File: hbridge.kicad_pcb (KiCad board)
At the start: 4 copper layers, 31.8 x 62.7 mm, 29 parts, among them J11 Conn_01x06_Male, J12 Screw_Terminal_01x04, J21 Conn_01x03_Male, J22 Conn_01x06_Female, Q1 2N7000, Q11 2N7000, Q13 2N3904, Q14 2N3906, Q15 2N3904, Q16 2N3906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

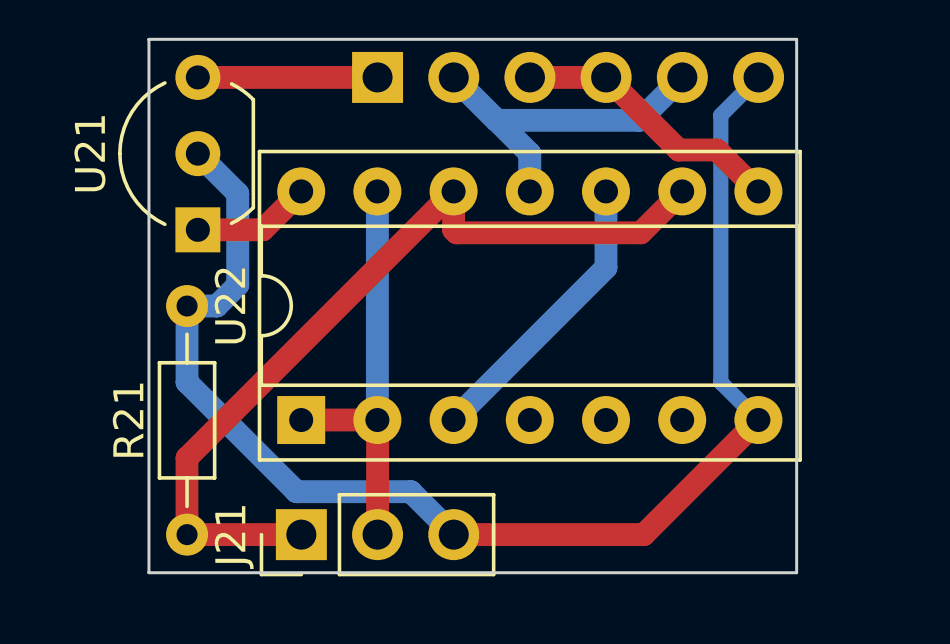
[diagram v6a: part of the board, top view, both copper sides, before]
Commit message: Added bypass cap, tied unused inputs to gnd
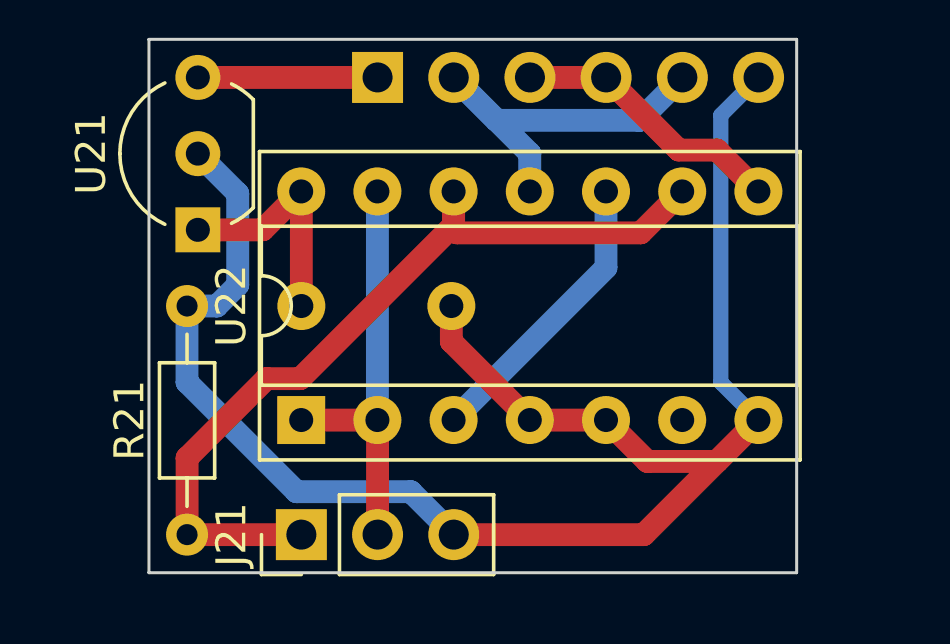
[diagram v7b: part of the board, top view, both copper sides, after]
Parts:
- added C21: 0.1u, Capacitor_THT:C_Disc_D4.3mm_W1.9mm_P5.00mm, B.Cu at (106.7, 109.2)
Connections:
- U22 pad 4: (no net) -> GND
- U22 pad 5: (no net) -> GND
- U22 pad 6: (no net) -> unconnected-(U22-Pad6)
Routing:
- net GND: track 163.0 -> 176.7 mm
- net +5V: track 3.98 -> 7.80 mm
- net /EN: track 28.4 -> 29.1 mm
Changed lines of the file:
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@@
   (net 17 "/DIR")
   (net 18 "Net-(U22-Pad10)")
+  (net 19 "unconnected-(U22-Pad6)")
   (footprint "Package_TO_SOT_THT:TO-220-3_Vertical" (layer "F.Cu")
     (at 115.245 80.01 90)
@@
     (pad "3" thru_hole oval (at 0 5.08 90) (size 1.6 1.6) (drill 0.8) (layers *.Cu *.Mask)
       (net 18 "Net-(U22-Pad10)") (pintype "output"))
-    (pad "4" thru_hole oval (at 0 7.62 90) (size 1.6 1.6) (drill 0.8) (layers *.Cu *.Mask))
-    (pad "5" thru_hole oval (at 0 10.16 90) (size 1.6 1.6) (drill 0.8) (layers *.Cu *.Mask))
-    (pad "6" thru_hole oval (at 0 12.7 90) (size 1.6 1.6) (drill 0.8) (layers *.Cu *.Mask))
+    (pad "4" thru_hole oval (at 0 7.62 90) (size 1.6 1.6) (drill 0.8) (layers *.Cu *.Mask)
+      (net 2 "GND") (pintype "input"))
+    (pad "5" thru_hole oval (at 0 10.16 90) (size 1.6 1.6) (drill 0.8) (layers *.Cu *.Mask)
+      (net 2 "GND") (pintype "input"))
+    (pad "6" thru_hole oval (at 0 12.7 90) (size 1.6 1.6) (drill 0.8) (layers *.Cu *.Mask)
+      (net 19 "unconnected-(U22-Pad6)") (pintype "output+no_connect"))
     (pad "7" thru_hole oval (at 0 15.24 90) (size 1.6 1.6) (drill 0.8) (layers *.Cu *.Mask)
       (net 2 "GND") (pinfunction "GND") (pintype "power_in"))
@@
     )
   )
+  (footprint "Capacitor_THT:C_Disc_D4.3mm_W1.9mm_P5.00mm" (layer "B.Cu")
+    (at 106.68 109.22)
+    (descr "C, Disc series, Radial, pin pitch=5.00mm, , diameter*width=4.3*1.9mm^2, Capacitor, http://www.vishay.com/docs/45233/krseries.pdf")
+    (tags "C Disc series Radial pin pitch 5.00mm  diameter 4.3mm width 1.9mm Capacitor")
+    (property "Sheetfile" "logic.kicad_sch")
+    (property "Sheetname" "control_logic")
+    (attr through_hole)
+    (fp_text reference "C21" (at 2.5 2.2) (layer "B.SilkS")
+      (effects (font (size 1 1) (thickness 0.15)) (justify mirror))
+    )
+    (fp_text value "0.1u" (at 2.5 -2.2) (layer "B.Fab")
+      (effects (font (size 1 1) (thickness 0.15)) (justify mirror))
+    )
+    (fp_text user "${REFERENCE}" (at 2.5 0) (layer "B.Fab")
+      (effects (font (size 0.86 0.86) (thickness 0.129)) (justify mirror))
+    )
+    (fp_line (start 0.23 -1.055) (end 0.23 -1.07) (layer "B.SilkS") (width 0.12))
+    (fp_line (start 0.23 1.07) (end 0.23 1.055) (layer "B.SilkS") (width 0.12))
+    (fp_line (start 4.77 -1.055) (end 4.77 -1.07) (layer "B.SilkS") (width 0.12))
+    (fp_line (start 4.77 1.07) (end 4.77 1.055) (layer "B.SilkS") (width 0.12))
+    (fp_line (start 0.23 -1.07) (end 4.77 -1.07) (layer "B.SilkS") (width 0.12))
+    (fp_line (start 0.23 1.07) (end 4.77 1.07) (layer "B.SilkS") (width 0.12))
+    (fp_line (start -1.05 1.2) (end -1.05 -1.2) (layer "B.CrtYd") (width 0.05))
+    (fp_line (start 6.05 1.2) (end -1.05 1.2) (layer "B.CrtYd") (width 0.05))
+    (fp_line (start 6.05 -1.2) (end 6.05 1.2) (layer "B.CrtYd") (width 0.05))
+    (fp_line (start -1.05 -1.2) (end 6.05 -1.2) (layer "B.CrtYd") (width 0.05))
+    (fp_line (start 4.65 -0.95) (end 4.65 0.95) (layer "B.Fab") (width 0.1))
+    (fp_line (start 0.35 -0.95) (end 4.65 -0.95) (layer "B.Fab") (width 0.1))
+    (fp_line (start 0.35 0.95) (end 0.35 -0.95) (layer "B.Fab") (width 0.1))
+    (fp_line (start 4.65 0.95) (end 0.35 0.95) (layer "B.Fab") (width 0.1))
+    (pad "1" thru_hole circle (at 0 0) (size 1.6 1.6) (drill 0.8) (layers *.Cu *.Mask)
+      (net 4 "+5V") (pintype "passive"))
+    (pad "2" thru_hole circle (at 5 0) (size 1.6 1.6) (drill 0.8) (layers *.Cu *.Mask)
+      (net 2 "GND") (pintype "passive"))
+    (model "${KICAD6_3DMODEL_DIR}/Capacitor_THT.3dshapes/C_Disc_D4.3mm_W1.9mm_P5.00mm.wrl"
+      (offset (xyz 0 0 0))
+      (scale (xyz 1 1 1))
+      (rotate (xyz 0 0 0))
+    )
+  )
   (footprint "Capacitor_SMD:C_0603_1608Metric" (layer "B.Cu")
     (at 114.3 57.263 -90)
@@
   (segment (start 118.237 87.757) (end 114.173 87.757) (width 0.762) (layer "F.Cu") (net 2))
   (segment (start 111.755489 65.536511) (end 111.755489 61.947989) (width 0.762) (layer "F.Cu") (net 2))
+  (segment (start 118.215511 114.400511) (end 120.534489 114.400511) (width 0.762) (layer "F.Cu") (net 2))
   (segment (start 109.982 67.31) (end 109.982 69.183559) (width 0.762) (layer "F.Cu") (net 2))
-  (segment (start 118.095 116.84) (end 121.915 113.02) (width 0.762) (layer "F.Cu") (net 2))
+  (segment (start 118.095 116.84) (end 121.9125 113.0225) (width 0.762) (layer "F.Cu") (net 2))
   (segment (start 121.92 61.468) (end 114.3 61.468) (width 0.762) (layer "F.Cu") (net 2))
   (segment (start 109.982 67.31) (end 111.252 68.58) (width 0.762) (layer "F.Cu") (net 2))
@@
   (segment (start 107.95 87.63) (end 114.046 87.63) (width 0.762) (layer "F.Cu") (net 2))
   (segment (start 126.365 90.805) (end 126.365 90.143223) (width 0.762) (layer "F.Cu") (net 2))
+  (segment (start 121.9125 113.0225) (end 121.915 113.02) (width 0.762) (layer "F.Cu") (net 2))
   (segment (start 119.770011 82.178011) (end 118.379997 80.787997) (width 2.032) (layer "F.Cu") (net 2))
+  (segment (start 116.84 113.025) (end 116.835 113.02) (width 0.762) (layer "F.Cu") (net 2))
   (segment (start 126.365 90.143223) (end 124.3584 88.136623) (width 0.762) (layer "F.Cu") (net 2))
   (segment (start 128.27 79.89) (end 125.981989 82.178011) (width 2.032) (layer "F.Cu") (net 2))
@@
   (segment (start 127 87.63) (end 132.08 87.63) (width 0.762) (layer "F.Cu") (net 2))
   (segment (start 125.981989 82.178011) (end 119.770011 82.178011) (width 2.032) (layer "F.Cu") (net 2))
+  (segment (start 116.83 113.02) (end 116.84 113.03) (width 0.762) (layer "F.Cu") (net 2))
+  (segment (start 111.68 110.405) (end 114.295 113.02) (width 0.762) (layer "F.Cu") (net 2))
   (segment (start 107.061 62.23) (end 107.061 63.870559) (width 0.762) (layer "F.Cu") (net 2))
   (segment (start 125.095 56.515) (end 130.45 56.515) (width 0.762) (layer "F.Cu") (net 2))
@@
   (segment (start 111.76 116.84) (end 118.095 116.84) (width 0.762) (layer "F.Cu") (net 2))
   (segment (start 114.046 87.63) (end 114.173 87.757) (width 0.762) (layer "F.Cu") (net 2))
+  (segment (start 116.84 113.03) (end 116.84 113.025) (width 0.762) (layer "F.Cu") (net 2))
   (segment (start 121.412 90.932) (end 118.237 87.757) (width 0.762) (layer "F.Cu") (net 2))
+  (segment (start 120.534489 114.400511) (end 121.9125 113.0225) (width 0.762) (layer "F.Cu") (net 2))
   (segment (start 109.982 69.183559) (end 107.315 71.850559) (width 0.762) (layer "F.Cu") (net 2))
   (segment (start 111.755489 61.947989) (end 112.235478 61.468) (width 0.762) (layer "F.Cu") (net 2))
+  (segment (start 111.68 109.22) (end 111.68 110.405) (width 0.762) (layer "F.Cu") (net 2))
   (segment (start 118.379997 80.787997) (end 118.379997 69.580003) (width 2.032) (layer "F.Cu") (net 2))
   (segment (start 107.061 63.870559) (end 109.982 66.791559) (width 0.762) (layer "F.Cu") (net 2))
   (segment (start 109.982 67.31) (end 111.755489 65.536511) (width 0.762) (layer "F.Cu") (net 2))
+  (segment (start 116.835 113.02) (end 118.215511 114.400511) (width 0.762) (layer "F.Cu") (net 2))
+  (segment (start 114.295 113.02) (end 116.83 113.02) (width 0.762) (layer "F.Cu") (net 2))
   (via (at 124.3584 88.0364) (size 0.8) (drill 0.4) (layers "F.Cu" "B.Cu") (free) (net 2))
   (via (at 115.57 63.5) (size 0.8) (drill 0.4) (layers "F.Cu" "B.Cu") (free) (net 2))
@@
   (segment (start 115.57052 67.681977) (end 113.928543 66.04) (width 2.032) (layer "B.Cu") (net 3))
   (segment (start 103.23 106.68) (end 105.395 106.68) (width 0.762) (layer "F.Cu") (net 4))
+  (segment (start 106.68 109.22) (end 106.68 105.405) (width 0.762) (layer "F.Cu") (net 4))
   (segment (start 105.395 106.68) (end 106.675 105.4) (width 0.762) (layer "F.Cu") (net 4))
+  (segment (start 106.68 105.405) (end 106.675 105.4) (width 0.762) (layer "F.Cu") (net 4))
   (segment (start 120.396 66.04) (end 119.38 66.04) (width 2.032) (layer "F.Cu") (net 5))
   (segment (start 121.611519 74.913481) (end 121.611519 67.255519) (width 2.032) (layer "F.Cu") (net 5))
@@
   (segment (start 125.095 59.055) (end 120.015 59.055) (width 0.762) (layer "B.Cu") (net 15))
   (segment (start 111.860511 106.780511) (end 111.755 106.675) (width 0.762) (layer "F.Cu") (net 16))
+  (segment (start 105.515511 111.639489) (end 106.646881 111.639489) (width 0.762) (layer "F.Cu") (net 16))
   (segment (start 117.994489 106.780511) (end 111.860511 106.780511) (width 0.762) (layer "F.Cu") (net 16))
   (segment (start 119.375 105.4) (end 117.994489 106.780511) (width 0.762) (layer "F.Cu") (net 16))
+  (segment (start 106.646881 111.639489) (end 111.755 106.53137) (width 0.762) (layer "F.Cu") (net 16))
   (segment (start 102.87 114.285) (end 102.87 116.84) (width 0.762) (layer "F.Cu") (net 16))
   (segment (start 111.755 106.675) (end 111.755 105.4) (width 0.762) (layer "F.Cu") (net 16))
-  (segment (start 111.755 105.4) (end 102.87 114.285) (width 0.762) (layer "F.Cu") (net 16))
   (segment (start 106.68 116.84) (end 102.87 116.84) (width 0.762) (layer "F.Cu") (net 16))
+  (segment (start 102.87 114.285) (end 105.515511 111.639489) (width 0.762) (layer "F.Cu") (net 16))
+  (segment (start 111.755 106.53137) (end 111.755 105.4) (width 0.762) (layer "F.Cu") (net 16))
   (segment (start 109.22 113.025) (end 109.215 113.02) (width 0.762) (layer "F.Cu") (net 17))
   (segment (start 109.215 113.02) (end 106.675 113.02) (width 0.762) (layer "F.Cu") (net 17))

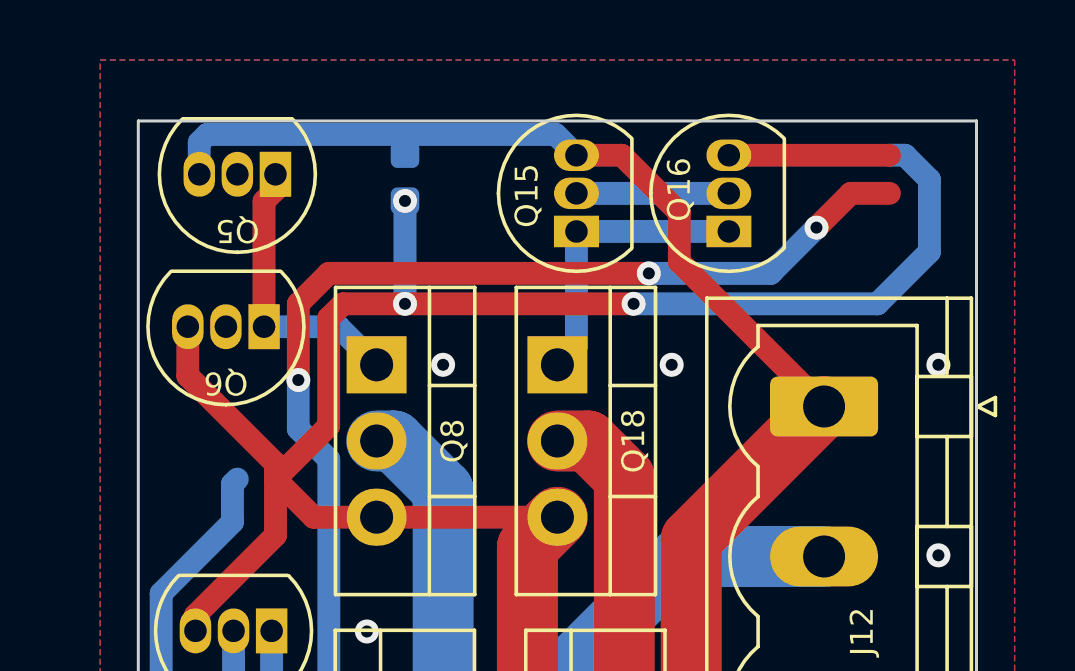
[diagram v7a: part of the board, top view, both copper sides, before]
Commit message: Rerouted greenwires
Found a simpler way to modify board
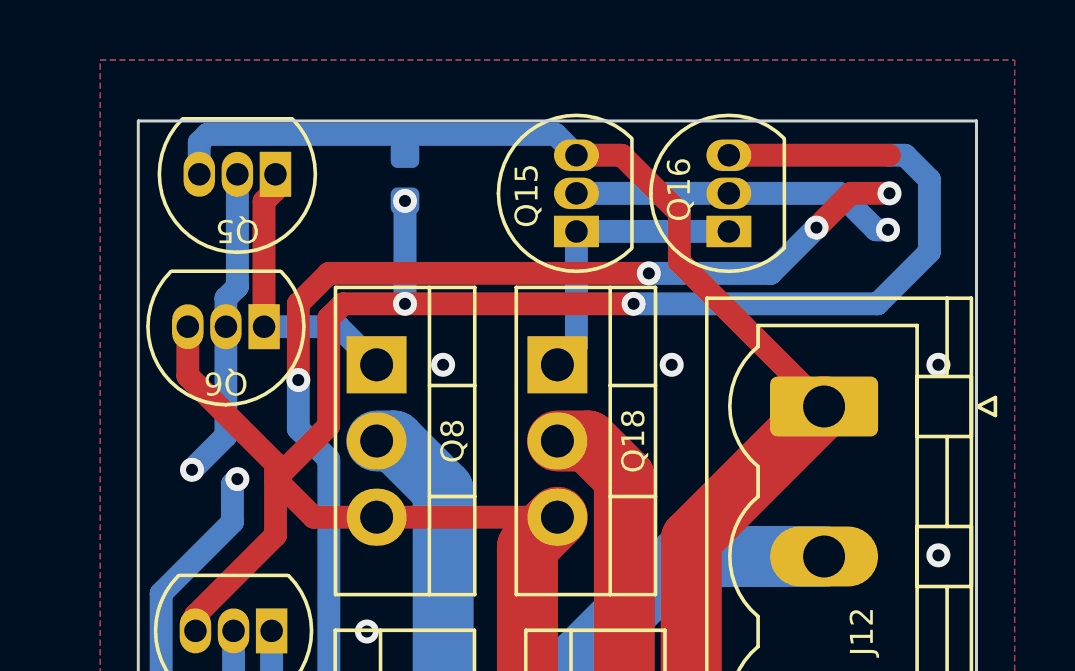
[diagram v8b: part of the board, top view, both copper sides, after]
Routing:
- net GND: track 176.7 -> 187.5 mm
- net +12V: track 98.2 -> 109.0 mm
- net /H2: track 117.5 -> 113.5 mm, vias 5 -> 7
- net /H1: track 88.4 -> 90.8 mm, vias 1 -> 3
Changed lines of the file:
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@@
     (pts (xy 133.35 55.372) (xy 133.35 92.456))
     (height -5.08)
-    (gr_text "1460.0000 mils" (at 137.28 73.914 90) (layer "Dwgs.User")
+    (gr_text "1.4600 in" (at 137.28 73.914 90) (layer "Dwgs.User")
       (effects (font (size 1 1) (thickness 0.15)))
     )
@@
     (pts (xy 105.41 54.61) (xy 133.35 54.61))
     (height -3.175)
-    (gr_text "1100.0000 mils" (at 119.38 50.285) (layer "Dwgs.User")
+    (gr_text "1.1000 in" (at 119.38 50.285) (layer "Dwgs.User")
       (effects (font (size 1 1) (thickness 0.15)))
     )
@@
   (segment (start 108.712 90.932) (end 109.228951 90.932) (width 0.762) (layer "In1.Cu") (net 1))
   (segment (start 109.228951 90.932) (end 115.832951 84.328) (width 0.762) (layer "In1.Cu") (net 1))
+  (segment (start 108.712 101.092) (end 109.22 101.6) (width 0.762) (layer "In1.Cu") (net 1))
   (segment (start 115.832951 84.328) (end 118.872 84.328) (width 0.762) (layer "In1.Cu") (net 1))
+  (segment (start 108.712 90.932) (end 108.712 101.092) (width 0.762) (layer "In1.Cu") (net 1))
   (segment (start 107.442 57.15) (end 107.442 56.088) (width 0.762) (layer "B.Cu") (net 1))
   (segment (start 119.319489 55.819489) (end 120.015 56.515) (width 0.762) (layer "B.Cu") (net 1))
@@
   (via (at 132.08 74.93) (size 0.8) (drill 0.4) (layers "F.Cu" "B.Cu") (free) (net 2))
   (via (at 114.3 61.468) (size 0.8) (drill 0.4) (layers "F.Cu" "B.Cu") (net 2))
+  (segment (start 121.412 101.092) (end 121.92 101.6) (width 0.762) (layer "In1.Cu") (net 2))
+  (segment (start 121.412 90.932) (end 121.412 101.092) (width 0.762) (layer "In1.Cu") (net 2))
   (segment (start 121.92 101.6) (end 120.661489 102.858511) (width 0.508) (layer "B.Cu") (net 2))
   (segment (start 114.173 88.024) (end 114.173 87.757) (width 0.762) (layer "B.Cu") (net 2))
@@
   (segment (start 117.348 89.408) (end 118.872 90.932) (width 0.762) (layer "F.Cu") (net 6))
   (via (at 109.22 89.408) (size 0.8) (drill 0.4) (layers "F.Cu" "B.Cu") (net 6))
-  (segment (start 105.95548 60.96852) (end 105.95548 84.883921) (width 0.762) (layer "In1.Cu") (net 6))
-  (segment (start 108.712 57.15) (end 108.712 58.212) (width 0.762) (layer "In1.Cu") (net 6))
-  (segment (start 105.95548 84.883921) (end 107.431559 86.36) (width 0.762) (layer "In1.Cu") (net 6))
-  (segment (start 107.431559 86.36) (end 107.95 86.36) (width 0.762) (layer "In1.Cu") (net 6))
-  (segment (start 108.712 58.212) (end 105.95548 60.96852) (width 0.762) (layer "In1.Cu") (net 6))
+  (via (at 107.2 67) (size 0.8) (drill 0.4) (layers "F.Cu" "B.Cu") (net 6))
+  (via (at 108.712 67.31) (size 0.8) (drill 0.4) (layers "F.Cu" "B.Cu") (net 6))
+  (segment (start 111.252 90.932) (end 111.252 101.092) (width 0.762) (layer "In1.Cu") (net 6))
+  (segment (start 108.402 67) (end 108.712 67.31) (width 0.762) (layer "In1.Cu") (net 6))
+  (segment (start 118.872 101.092) (end 119.38 101.6) (width 0.762) (layer "In1.Cu") (net 6))
+  (segment (start 118.872 90.932) (end 118.872 101.092) (width 0.762) (layer "In1.Cu") (net 6))
+  (segment (start 107.2 67) (end 108.402 67) (width 0.762) (layer "In1.Cu") (net 6))
+  (segment (start 111.252 101.092) (end 111.76 101.6) (width 0.762) (layer "In1.Cu") (net 6))
   (segment (start 114.295 104.135) (end 111.76 101.6) (width 0.762) (layer "B.Cu") (net 6))
   (segment (start 111.252 90.932) (end 111.252 88.15) (width 0.762) (layer "B.Cu") (net 6))
+  (segment (start 108.331 65.869) (end 107.2 67) (width 0.762) (layer "B.Cu") (net 6))
   (segment (start 117.949489 103.030511) (end 119.38 101.6) (width 0.762) (layer "B.Cu") (net 6))
   (segment (start 109.462 86.36) (end 107.95 86.36) (width 0.762) (layer "B.Cu") (net 6))
   (segment (start 106.172 89.408) (end 109.22 89.408) (width 0.762) (layer "B.Cu") (net 6))
   (segment (start 111.76 101.6) (end 113.190511 103.030511) (width 0.762) (layer "B.Cu") (net 6))
+  (segment (start 108.712 60.899) (end 108.331 61.28) (width 0.762) (layer "B.Cu") (net 6))
+  (segment (start 108.331 61.28) (end 108.331 62.23) (width 0.762) (layer "B.Cu") (net 6))
+  (segment (start 108.712 57.15) (end 108.712 60.899) (width 0.762) (layer "B.Cu") (net 6))
   (segment (start 111.252 88.15) (end 109.462 86.36) (width 0.762) (layer "B.Cu") (net 6))
   (segment (start 108.54752 67.47448) (end 108.54752 68.74448) (width 0.762) (layer "B.Cu") (net 6))
@@
   (segment (start 108.712 67.31) (end 108.54752 67.47448) (width 0.762) (layer "B.Cu") (net 6))
   (segment (start 113.190511 103.030511) (end 117.949489 103.030511) (width 0.762) (layer "B.Cu") (net 6))
+  (segment (start 108.331 62.23) (end 108.331 65.869) (width 0.762) (layer "B.Cu") (net 6))
   (segment (start 108.54752 68.74448) (end 106.172 71.12) (width 0.762) (layer "B.Cu") (net 6))
   (segment (start 114.295 105.4) (end 114.295 104.135) (width 0.762) (layer "B.Cu") (net 6))
@@
   (via (at 122.428 60.452) (size 0.8) (drill 0.4) (layers "F.Cu" "B.Cu") (net 7))
   (via (at 110.744 77.216) (size 0.8) (drill 0.4) (layers "F.Cu" "B.Cu") (net 7))
-  (segment (start 127.035489 58.559467) (end 127.035489 60.180957) (width 0.762) (layer "In1.Cu") (net 7))
-  (segment (start 125.095 57.785) (end 126.261022 57.785) (width 0.762) (layer "In1.Cu") (net 7))
-  (segment (start 130.749489 86.045489) (end 131.064 86.36) (width 0.762) (layer "In1.Cu") (net 7))
-  (segment (start 126.261022 57.785) (end 127.035489 58.559467) (width 0.762) (layer "In1.Cu") (net 7))
-  (segment (start 127.035489 60.180957) (end 130.749489 63.894957) (width 0.762) (layer "In1.Cu") (net 7))
-  (segment (start 131.064 86.36) (end 132.08 86.36) (width 0.762) (layer "In1.Cu") (net 7))
-  (segment (start 130.749489 63.894957) (end 130.749489 86.045489) (width 0.762) (layer "In1.Cu") (net 7))
+  (via (at 130.4 59) (size 0.8) (drill 0.4) (layers "F.Cu" "B.Cu") (net 7))
+  (via (at 130.45 57.785) (size 0.8) (drill 0.4) (layers "F.Cu" "B.Cu") (net 7))
+  (segment (start 113.792 101.092) (end 114.3 101.6) (width 0.762) (layer "In1.Cu") (net 7))
+  (segment (start 116.332 90.932) (end 116.332 101.092) (width 0.762) (layer "In1.Cu") (net 7))
+  (segment (start 113.792 90.932) (end 113.792 101.092) (width 0.762) (layer "In1.Cu") (net 7))
+  (segment (start 130.45 58.95) (end 130.4 59) (width 0.762) (layer "In1.Cu") (net 7))
+  (segment (start 130.45 57.785) (end 130.45 58.95) (width 0.762) (layer "In1.Cu") (net 7))
+  (segment (start 116.332 101.092) (end 116.84 101.6) (width 0.762) (layer "In1.Cu") (net 7))
   (segment (start 111.76 74.168) (end 111.76 66.651978) (width 0.762) (layer "B.Cu") (net 7))
   (segment (start 130.913978 86.36) (end 132.08 86.36) (width 0.762) (layer "B.Cu") (net 7))
   (segment (start 120.015 57.785) (end 125.095 57.785) (width 0.762) (layer "B.Cu") (net 7))
+  (segment (start 125.095 57.785) (end 128.785 57.785) (width 0.762) (layer "B.Cu") (net 7))
   (segment (start 112.942 79.414) (end 110.744 77.216) (width 0.762) (layer "B.Cu") (net 7))
   (segment (start 111.76 66.651978) (end 110.744 65.635978) (width 0.762) (layer "B.Cu") (net 7))
@@
   (segment (start 113.792 90.932) (end 112.942 90.082) (width 0.762) (layer "B.Cu") (net 7))
   (segment (start 126.492 60.452) (end 122.428 60.452) (width 0.762) (layer "B.Cu") (net 7))
+  (segment (start 130 59) (end 130.4 59) (width 0.762) (layer "B.Cu") (net 7))
+  (segment (start 128.785 57.785) (end 130 59) (width 0.762) (layer "B.Cu") (net 7))
   (segment (start 128.016 58.928) (end 126.492 60.452) (width 0.762) (layer "B.Cu") (net 7))
   (segment (start 127.865978 89.408) (end 130.913978 86.36) (width 0.762) (layer "B.Cu") (net 7))
